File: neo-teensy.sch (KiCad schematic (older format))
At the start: 18 parts, among them J10 Conn_01x14, J11 Conn_02x04_Odd_Even, J12 Conn_01x02, J3 Conn_01x14_Male, J5 Conn_01x05_Male, J7 Conn_01x14_Male, J8 Conn_02x07_Odd_Even, J9 Conn_01x01_Male, U1 SN74AHCT125N

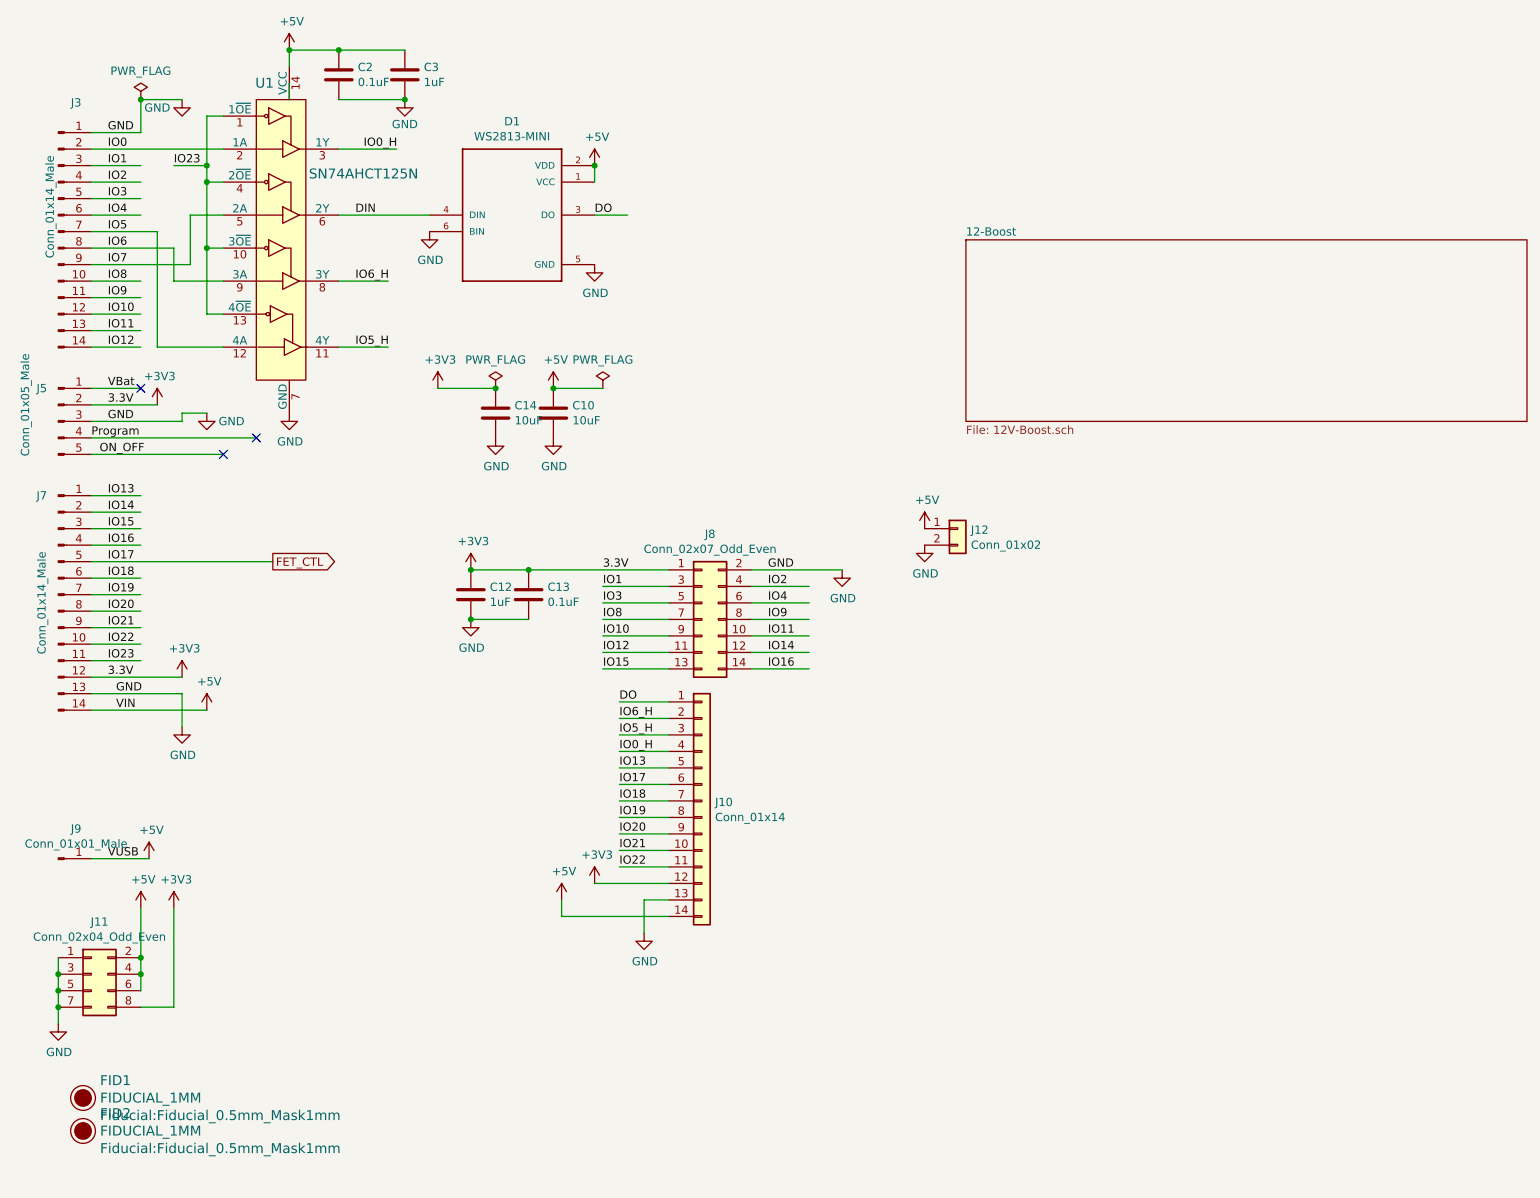
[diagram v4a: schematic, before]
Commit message: Changed GPIOs for Teensy 4.0
The 5V GPIOs were changed for the Teensy 4.0.  In addition the GPIOs to
the 14 pin header were also changed.

Some component values were also changed for the power supply.

Note that this is still compatible with the 3.1 stencil.

This also fixes the 12V BOM.

Signed-off-by: Aaron Williams <aaron.w2@gmail.com>
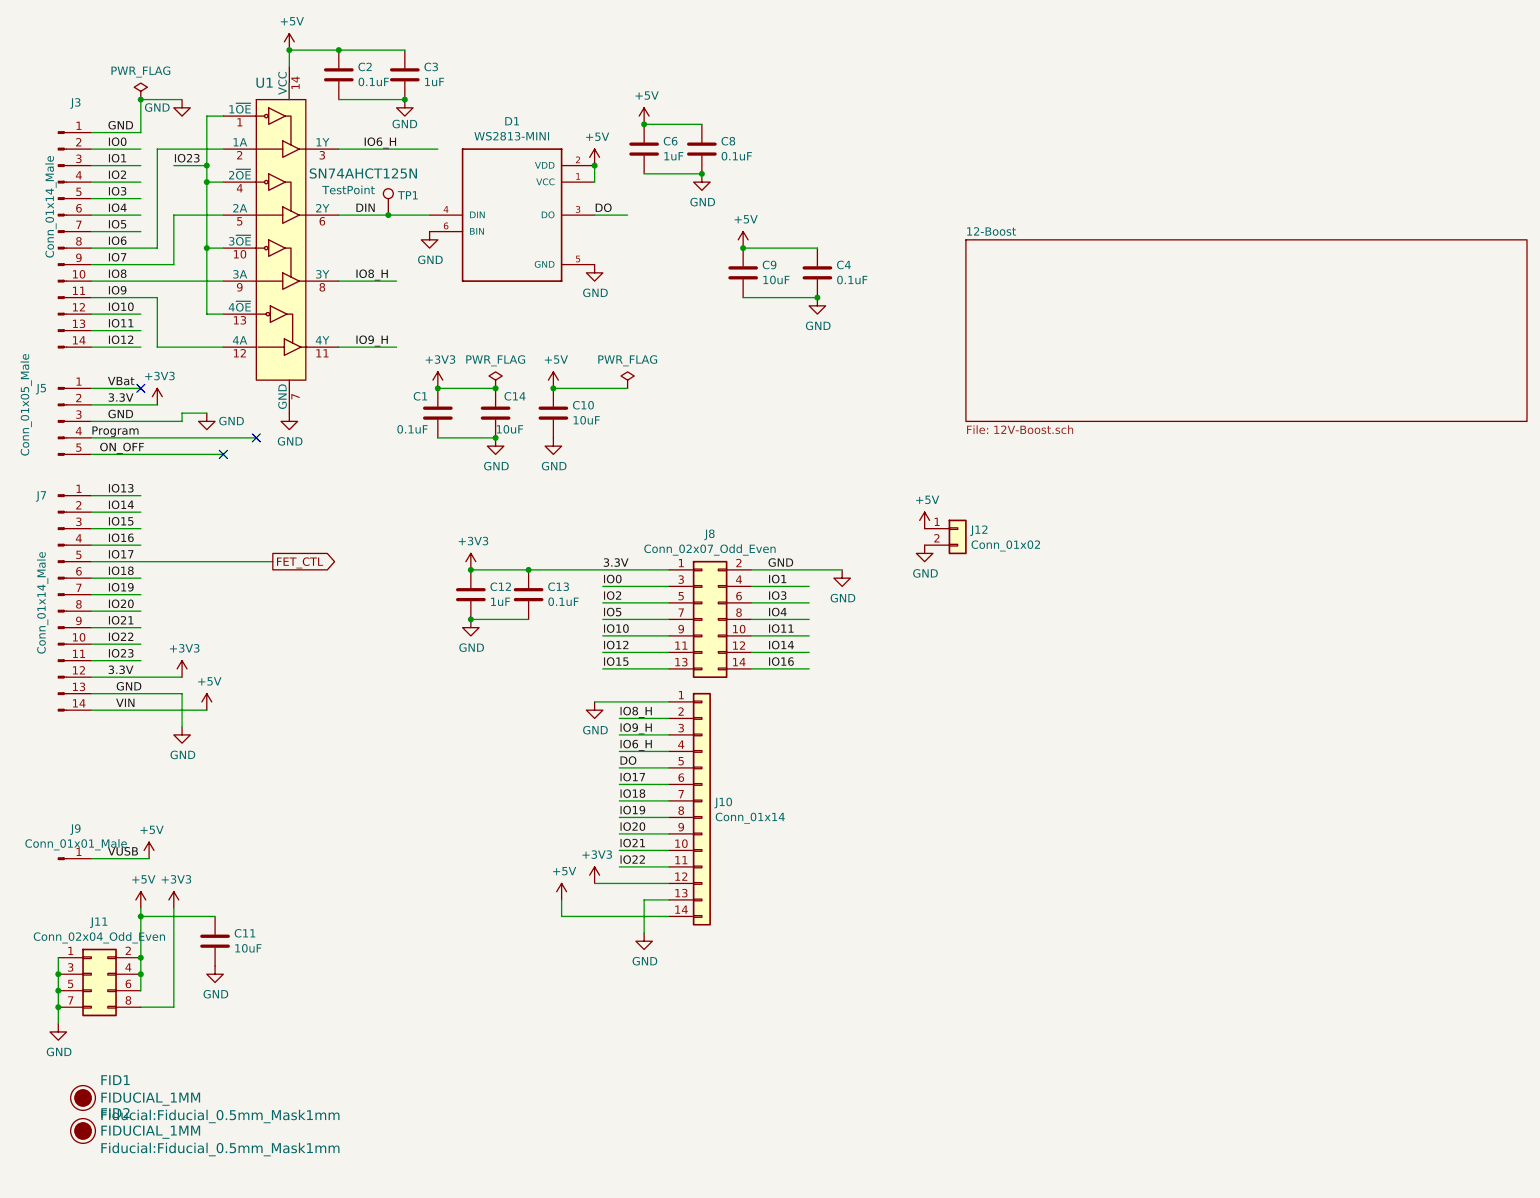
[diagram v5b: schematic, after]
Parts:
- added C1, C4, C8: 0.1uF, Capacitor_SMD:C_0603_1608Metric, symbol Device:C
- added C11, C9: 10uF, Capacitor_SMD:C_0805_2012Metric, symbol Device:C
- added C6: 1uF, Capacitor_SMD:C_0603_1608Metric, symbol Device:C
- added TP1: TestPoint, TestPoint:TestPoint_Pad_D1.0mm, symbol Connector:TestPoint
- C10, C14: DESC (none) -> CAP CER 10UF 10V X7R 0805; SPURL - -> https://www.digikey.com/products/en?keywords=490-14381-1-ND
- C12, C3: DESC (none) -> CAP CER 1UF 25V X7R 0603; SPURL - -> https://www.digikey.com/products/en?keywords=1276-1184-1-ND
- C13, C2: DESC (none) -> CAP CER 0.1UF 16V X7R 0603; SPURL - -> https://www.digikey.com/products/en?keywords=1276-6582-1-ND
- D1: DESC (none) -> RGB 620~625nm Red, 515~525nm Green, 465~475nm Blue SMD-6 Li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; SPN - -> C189639; SPR - -> LCSC; SPURL - -> https://lcsc.com/product-detail/Others_WS2813-Mini-WS2813-3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
- FID1, FID2, J10, J11, J12, J3, J5, J7, J8, J9: DESC (none) -> -
- U1: DESC (none) -> IC BUF NON-INVERT 5.5V 14VQFN; SPURL - -> https://www.digikey.com/products/en?keywords=296-13910-1-ND
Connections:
- net labels added: IO8_H, IO9_H
- net labels removed: IO0_H, IO5_H
- wire segments 108 -> 116

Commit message: Added pull-up resistors to 14-pin header
Made board 4 layers

Made board double sided

Signed-off-by: Aaron Williams <aaron.w2@gmail.com>
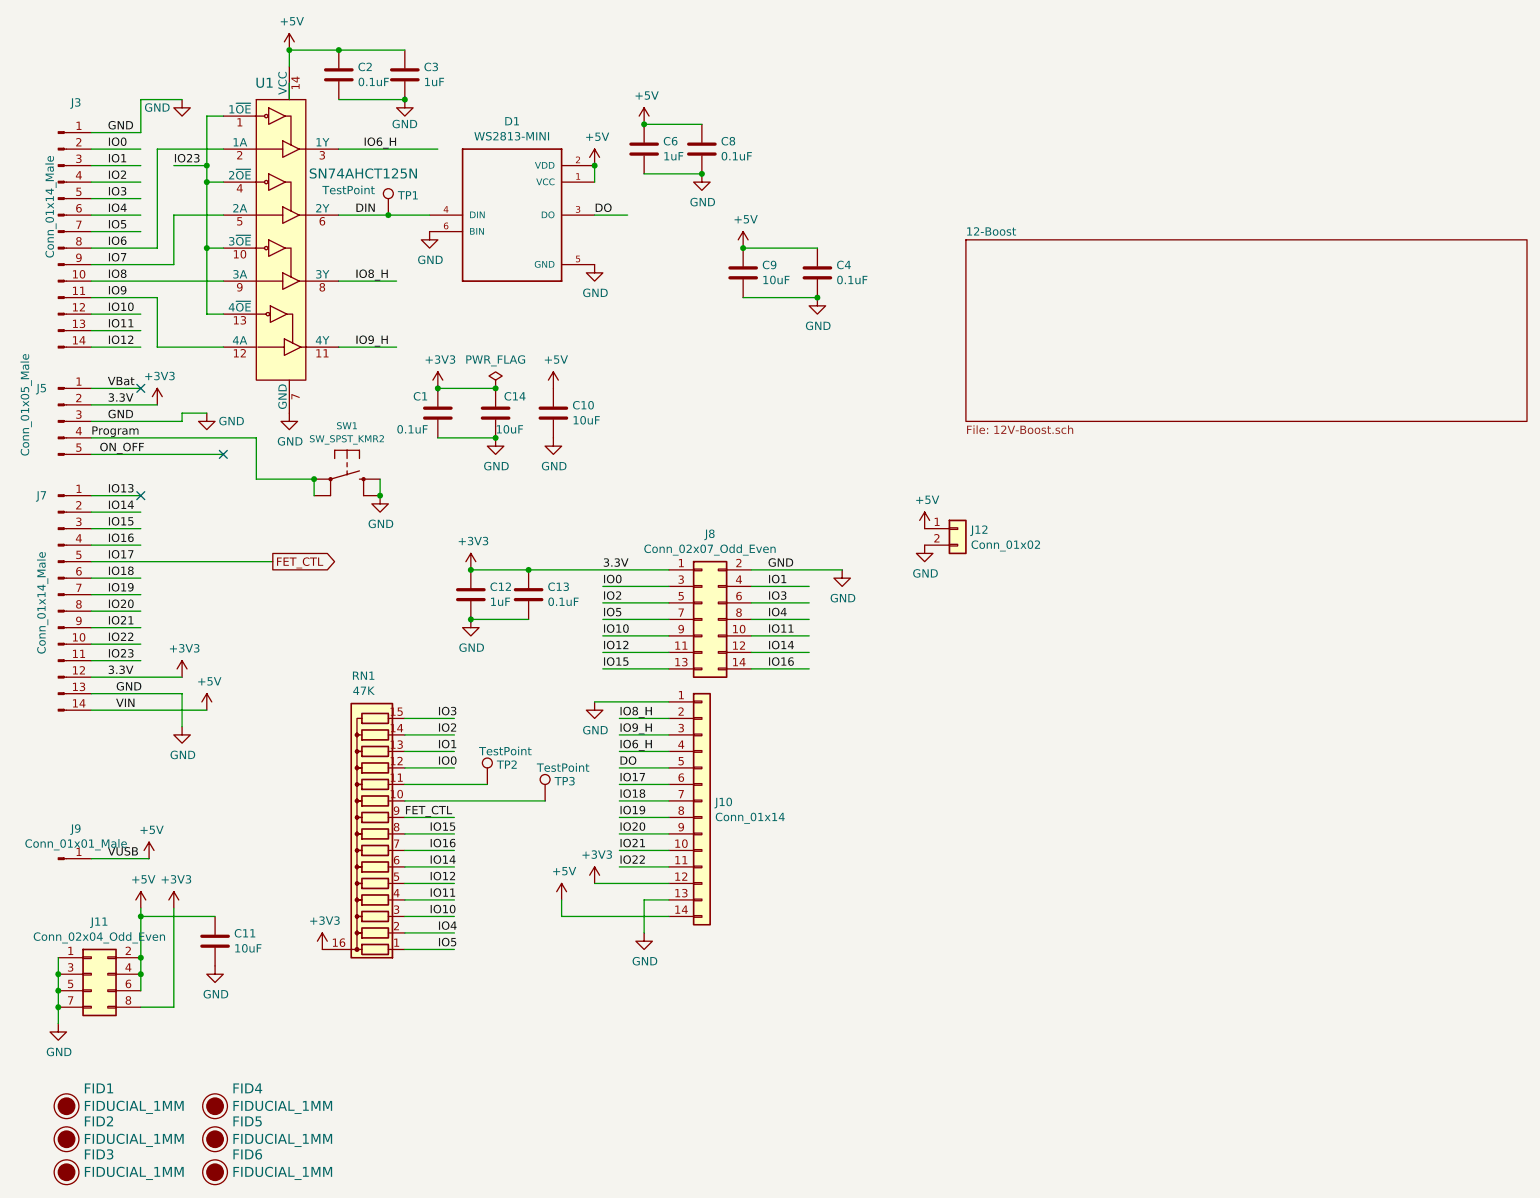
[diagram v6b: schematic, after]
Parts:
- added FID3, FID4, FID5, FID6: FIDUCIAL_1MM, Fiducial:Fiducial_0.5mm_Mask1mm, symbol fiducial:FIDUCIAL_1MM
- added RN1: 47K, Resistor_SMD:R_Array_Convex_8x0602, symbol Aaron:R_Network15
- added SW1: SW_SPST_KMR2, Aaron:SW_SPST_KMR2, symbol switch_tact_smt:SW_SPST_KMR2
- added TP2, TP3: TestPoint, TestPoint:TestPoint_Pad_D1.0mm, symbol Connector:TestPoint
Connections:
- wire segments 116 -> 134
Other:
- moved on the sheet: FID1, FID2
